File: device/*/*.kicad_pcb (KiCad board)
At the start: 2 copper layers, 99.5 x 99.5 mm, 7 parts, among them SW1 SW_Push, SW2 SW_Push

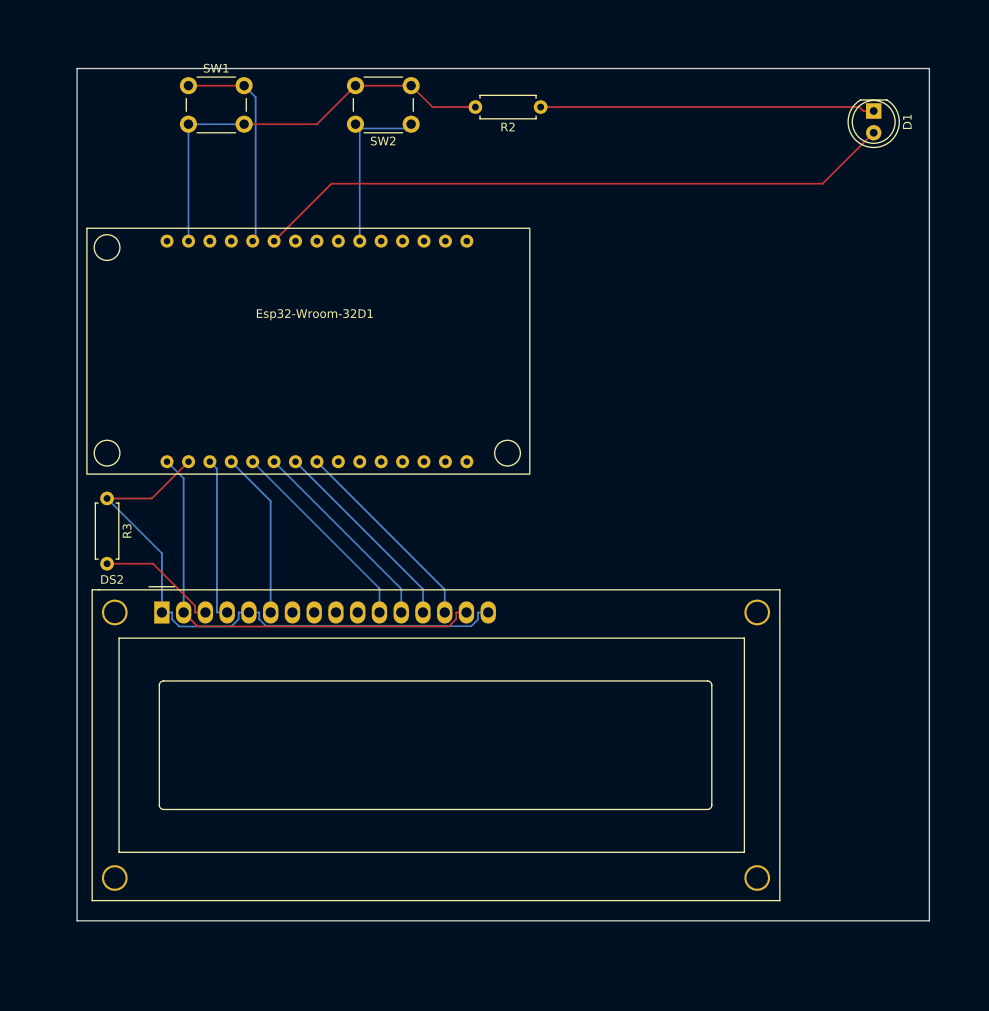
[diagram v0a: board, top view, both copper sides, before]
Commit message: feat: server send local time back
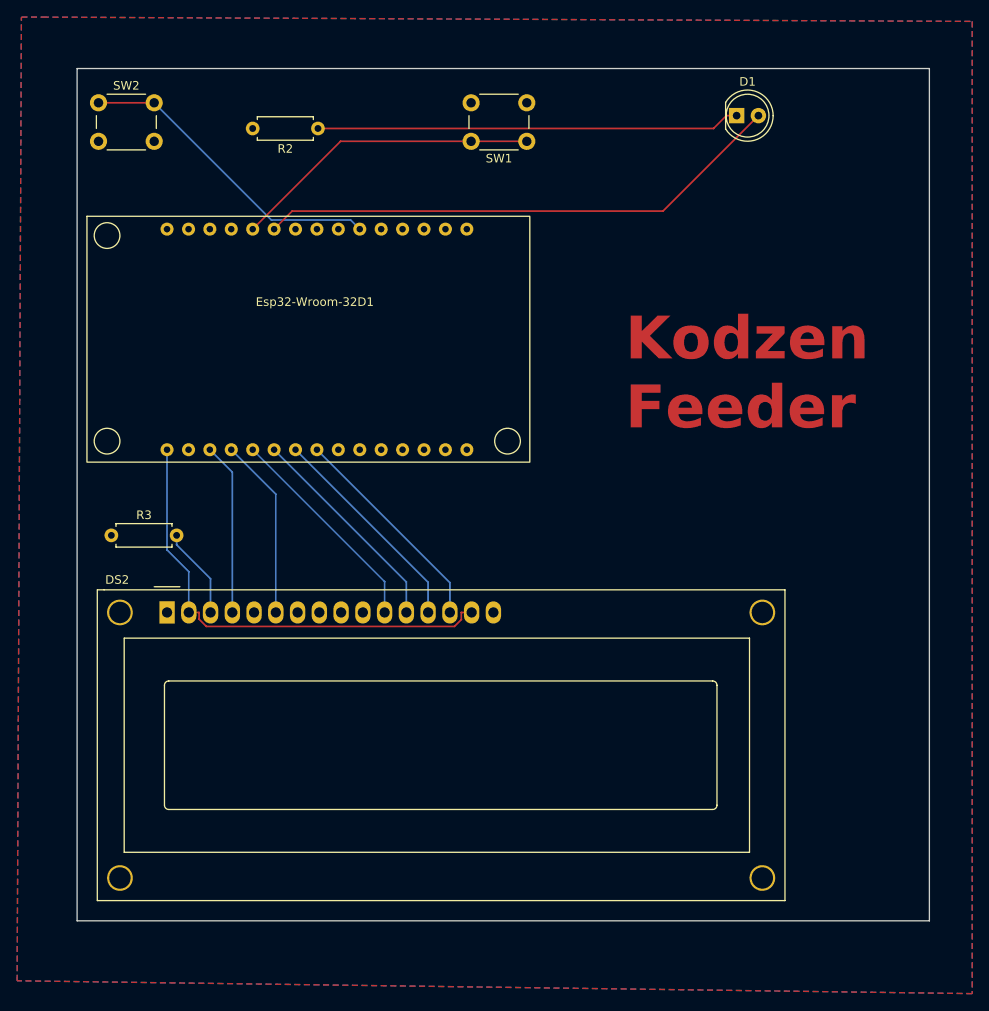
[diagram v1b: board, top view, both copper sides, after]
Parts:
- moved SW1 40.0 mm to (182.0, 51.5), turned to 180 degrees
- moved SW2 36.6 mm to (132.0, 47.0), turned to 0 degrees
- moved R2 26.1 mm to (157.6, 50.0)
- moved D1 16.0 mm to (206.5, 48.5), turned to 0 degrees
- moved R3 4.34 mm to (133.5, 97.5), turned to 0 degrees
- moved Esp32-Wroom-32D1 1.40 mm to (157.2, 70.8)
- moved DS2 0.60 mm to (140.0, 106.5)
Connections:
- DS2 pad 1: Net-(DS2-LED(-)) -> GND
- DS2 pad 16: Net-(DS2-LED(-)) -> GND
- DS2 pad 5: Net-(DS2-LED(-)) -> GND
- Esp32-Wroom-32D1 pad 1: Net-(Esp32-Wroom-32D1-GND-Pad1) -> GND
- Esp32-Wroom-32D1 pad 38: Net-(DS2-LED(-)) -> GND
- R2 pad 2: Net-(Esp32-Wroom-32D1-GND-Pad1) -> GND
- R3 pad 1: Net-(DS2-LED(-)) -> GND
- SW1 pad 2: Net-(Esp32-Wroom-32D1-GND-Pad1) -> GND
- SW2 pad 2: Net-(Esp32-Wroom-32D1-GND-Pad1) -> GND
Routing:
- net Net-(DS2-LED(-)): track 69.9 -> 0.00 mm
- net Net-(Esp32-Wroom-32D1-GND-Pad1): track 50.0 -> 0.00 mm
- net Net-(Esp32-Wroom-32D1-D32): track 20.1 -> 36.6 mm
- net Net-(D1-A): track 75.2 -> 62.0 mm
- net Net-(Esp32-Wroom-32D1-D14): track 25.3 -> 36.2 mm
- net Net-(D1-K): track 39.1 -> 49.5 mm
- net Net-(DS2-VO): track 14.3 -> 10.6 mm
- net Net-(DS2-LED(+)): track 53.2 -> 55.4 mm
- net Net-(DS2-D7): track 23.8 -> 25.4 mm
- net Net-(DS2-E): track 19.5 -> 21.2 mm
- net Net-(DS2-D6): track 23.8 -> 25.4 mm
- net Net-(DS2-D5): track 23.7 -> 25.4 mm
- net Net-(DS2-D4): track 23.7 -> 25.4 mm
- net Net-(DS2-RS): track 19.1 -> 20.1 mm
- added copper zone on B.Cu, net GND
- added copper zone on F.Cu, net GND
